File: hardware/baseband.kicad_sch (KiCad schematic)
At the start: 3 parts

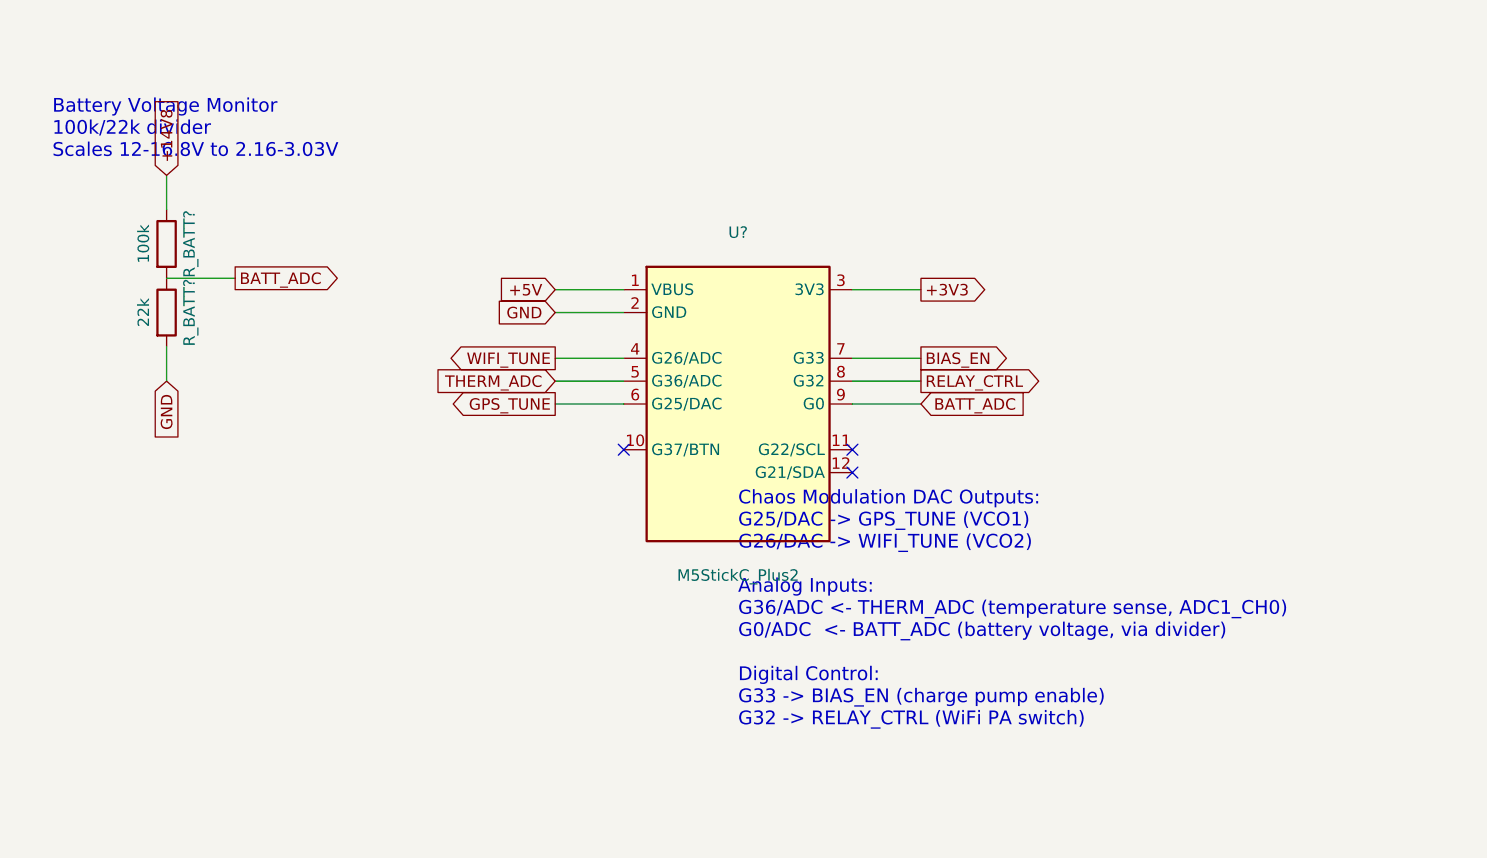
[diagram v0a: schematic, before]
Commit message: jamrf-v2: Add U3V70F15 WiFi PA regulator, FR408HR stackup, full firmware, custom footprints
- Add U3V70F15 buck-boost converter to limit WiFi PA supply to 15V (fixes ZVE-3W-83+ overvoltage)
- Update PCB stackup to Isola FR408HR (Er=3.65, tan d=0.0095) with corrected 0.40mm 50-ohm traces
- Add full operational firmware (main.py): chaos modulation engine, ST7789 display, mode control
- Add 6 custom footprints: M5StickC, Pololu D24V10F5/U3V70F15, Mini-Circuits, Wurth shield, isolator
- Add fp-lib-table and sym-lib-table for custom libraries
- Update README with logo, badges, TIIUAE disclaimer, corrected specs
- Update LICENSE with proper attribution

Co-Authored-By: Claude Opus 4.6 <noreply@anthropic.com>
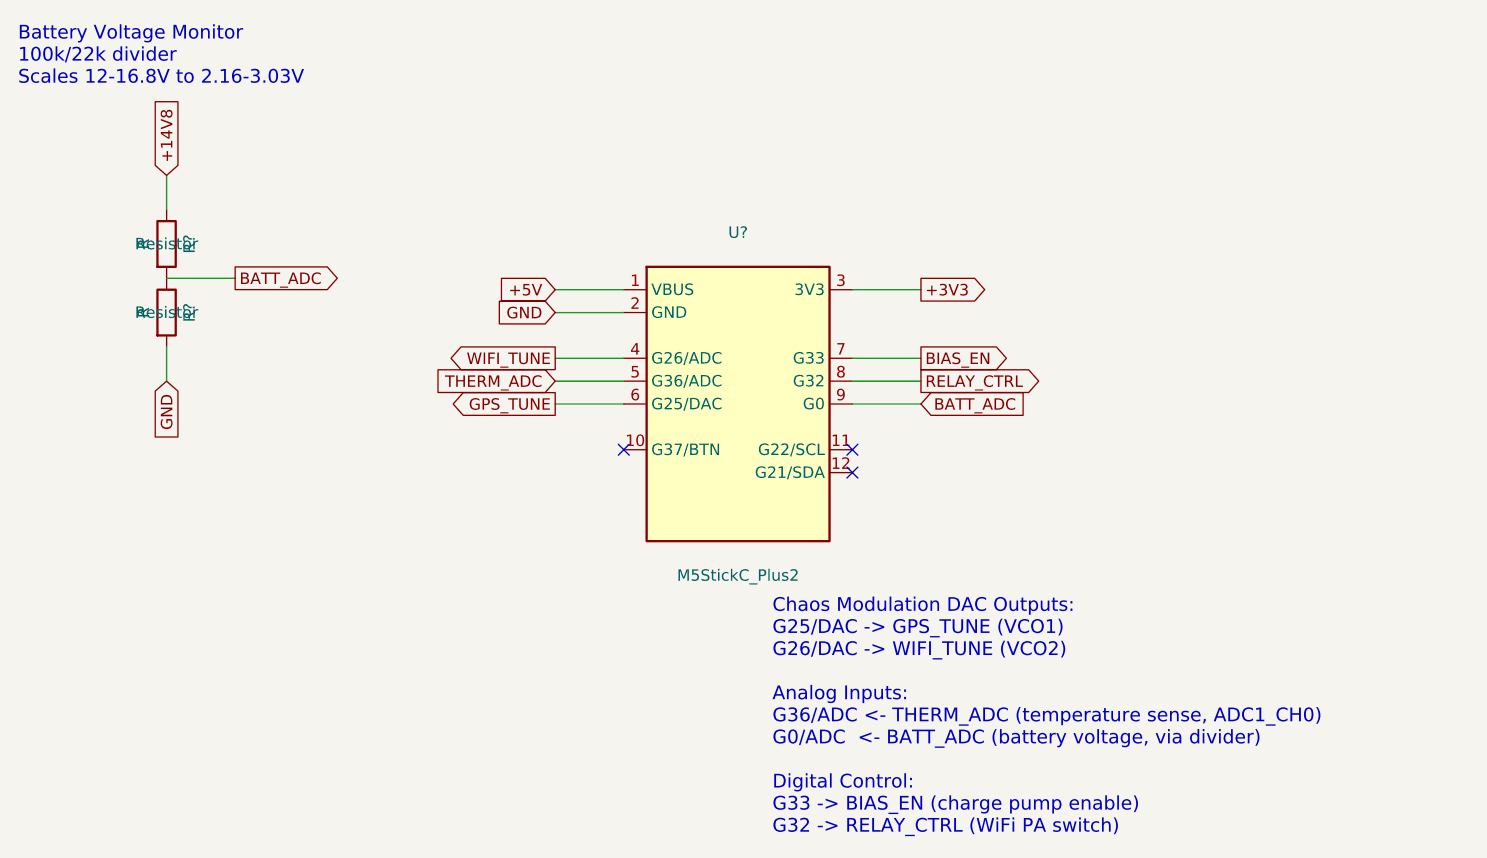
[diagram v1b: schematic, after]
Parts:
- R?: renamed from R_BATT?; value 100k -> R
- R?: renamed from R_BATT?; value 22k -> R
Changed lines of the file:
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@@
 	(text "Battery Voltage Monitor\n100k/22k divider\nScales 12-16.8V to 2.16-3.03V"
 		(exclude_from_sim no)
-		(at 63.5 58.42 0)
+		(at 59.69 50.292 0)
 		(effects
 			(font
@@
 	(text "Chaos Modulation DAC Outputs:\nG25/DAC -> GPS_TUNE (VCO1)\nG26/DAC -> WIFI_TUNE (VCO2)\n\nAnalog Inputs:\nG36/ADC <- THERM_ADC (temperature sense, ADC1_CH0)\nG0/ADC  <- BATT_ADC (battery voltage, via divider)\n\nDigital Control:\nG33 -> BIAS_EN (charge pump enable)\nG32 -> RELAY_CTRL (WiFi PA switch)"
 		(exclude_from_sim no)
-		(at 139.7 111.76 0)
+		(at 143.51 123.698 0)
 		(effects
 			(font
@@
 			(width 0)
 			(type default)
+		)
+	)
+	(global_label "+5V"
+		(shape input)
+		(at 119.38 76.2 180)
+		(effects
+			(font
+				(size 1.27 1.27)
+			)
+			(justify right)
+		)
+		(property "Intersheetrefs" "${INTERSHEET_REFS}"
+			(at 119.38 76.2 0)
+			(effects
+				(font
+					(size 1.27 1.27)
+				)
+				(hide yes)
+			)
+		)
+	)
+	(global_label "GND"
+		(shape input)
+		(at 119.38 78.74 180)
+		(effects
+			(font
+				(size 1.27 1.27)
+			)
+			(justify right)
+		)
+		(property "Intersheetrefs" "${INTERSHEET_REFS}"
+			(at 119.38 78.74 0)
+			(effects
+				(font
+					(size 1.27 1.27)
+				)
+				(hide yes)
+			)
+		)
+	)
+	(global_label "+3V3"
+		(shape output)
+		(at 160.02 76.2 0)
+		(effects
+			(font
+				(size 1.27 1.27)
+			)
+			(justify left)
+		)
+		(property "Intersheetrefs" "${INTERSHEET_REFS}"
+			(at 160.02 76.2 0)
+			(effects
+				(font
+					(size 1.27 1.27)
+				)
+				(hide yes)
+			)
+		)
+	)
+	(global_label "WIFI_TUNE"
+		(shape output)
+		(at 119.38 83.82 180)
+		(effects
+			(font
+				(size 1.27 1.27)
+			)
+			(justify right)
+		)
+		(property "Intersheetrefs" "${INTERSHEET_REFS}"
+			(at 119.38 83.82 0)
+			(effects
+				(font
+					(size 1.27 1.27)
+				)
+				(hide yes)
+			)
 		)
 	)
@@
 		)
 	)
+	(global_label "GPS_TUNE"
+		(shape output)
+		(at 119.38 88.9 180)
+		(effects
+			(font
+				(size 1.27 1.27)
+			)
+			(justify right)
+		)
+		(property "Intersheetrefs" "${INTERSHEET_REFS}"
+			(at 119.38 88.9 0)
+			(effects
+				(font
+					(size 1.27 1.27)
+				)
+				(hide yes)
+			)
+		)
+	)
+	(global_label "BIAS_EN"
+		(shape output)
+		(at 160.02 83.82 0)
+		(effects
+			(font
+				(size 1.27 1.27)
+			)
+			(justify left)
+		)
+		(property "Intersheetrefs" "${INTERSHEET_REFS}"
+			(at 160.02 83.82 0)
+			(effects
+				(font
+					(size 1.27 1.27)
+				)
+				(hide yes)
+			)
+		)
+	)
+	(global_label "RELAY_CTRL"
+		(shape output)
+		(at 160.02 86.36 0)
+		(effects
+			(font
+				(size 1.27 1.27)
+			)
+			(justify left)
+		)
+		(property "Intersheetrefs" "${INTERSHEET_REFS}"
+			(at 160.02 86.36 0)
+			(effects
+				(font
+					(size 1.27 1.27)
+				)
+				(hide yes)
+			)
+		)
+	)
+	(global_label "BATT_ADC"
+		(shape input)
+		(at 160.02 88.9 0)
+		(effects
+			(font
+				(size 1.27 1.27)
+			)
+			(justify left)
+		)
+		(property "Intersheetrefs" "${INTERSHEET_REFS}"
+			(at 160.02 88.9 0)
+			(effects
+				(font
+					(size 1.27 1.27)
+				)
+				(hide yes)
+			)
+		)
+	)
+	(global_label "+14V8"
+		(shape input)
+		(at 76.2 63.5 90)
+		(effects
+			(font
+				(size 1.27 1.27)
+			)
+			(justify left)
+		)
+		(property "Intersheetrefs" "${INTERSHEET_REFS}"
+			(at 76.2 63.5 0)
+			(effects
+				(font
+					(size 1.27 1.27)
+				)
+				(hide yes)
+			)
+		)
+	)
 	(global_label "BATT_ADC"
 		(shape output)
@@
 		(property "Intersheetrefs" "${INTERSHEET_REFS}"
 			(at 83.82 74.93 0)
-			(effects
-				(font
-					(size 1.27 1.27)
-				)
-				(hide yes)
-			)
-		)
-	)
-	(global_label "+5V"
-		(shape input)
-		(at 119.38 76.2 180)
-		(effects
-			(font
-				(size 1.27 1.27)
-			)
-			(justify right)
-		)
-		(property "Intersheetrefs" "${INTERSHEET_REFS}"
-			(at 119.38 76.2 0)
-			(effects
-				(font
-					(size 1.27 1.27)
-				)
-				(hide yes)
-			)
-		)
-	)
-	(global_label "GND"
-		(shape input)
-		(at 119.38 78.74 180)
-		(effects
-			(font
-				(size 1.27 1.27)
-			)
-			(justify right)
-		)
-		(property "Intersheetrefs" "${INTERSHEET_REFS}"
-			(at 119.38 78.74 0)
-			(effects
-				(font
-					(size 1.27 1.27)
-				)
-				(hide yes)
-			)
-		)
-	)
-	(global_label "+3V3"
-		(shape output)
-		(at 160.02 76.2 0)
-		(effects
-			(font
-				(size 1.27 1.27)
-			)
-			(justify left)
-		)
-		(property "Intersheetrefs" "${INTERSHEET_REFS}"
-			(at 160.02 76.2 0)
-			(effects
-				(font
-					(size 1.27 1.27)
-				)
-				(hide yes)
-			)
-		)
-	)
-	(global_label "WIFI_TUNE"
-		(shape output)
-		(at 119.38 83.82 180)
-		(effects
-			(font
-				(size 1.27 1.27)
-			)
-			(justify right)
-		)
-		(property "Intersheetrefs" "${INTERSHEET_REFS}"
-			(at 119.38 83.82 0)
-			(effects
-				(font
-					(size 1.27 1.27)
-				)
-				(hide yes)
-			)
-		)
-	)
-	(global_label "GPS_TUNE"
-		(shape output)
-		(at 119.38 88.9 180)
-		(effects
-			(font
-				(size 1.27 1.27)
-			)
-			(justify right)
-		)
-		(property "Intersheetrefs" "${INTERSHEET_REFS}"
-			(at 119.38 88.9 0)
-			(effects
-				(font
-					(size 1.27 1.27)
-				)
-				(hide yes)
-			)
-		)
-	)
-	(global_label "BIAS_EN"
-		(shape output)
-		(at 160.02 83.82 0)
-		(effects
-			(font
-				(size 1.27 1.27)
-			)
-			(justify left)
-		)
-		(property "Intersheetrefs" "${INTERSHEET_REFS}"
-			(at 160.02 83.82 0)
-			(effects
-				(font
-					(size 1.27 1.27)
-				)
-				(hide yes)
-			)
-		)
-	)
-	(global_label "RELAY_CTRL"
-		(shape output)
-		(at 160.02 86.36 0)
-		(effects
-			(font
-				(size 1.27 1.27)
-			)
-			(justify left)
-		)
-		(property "Intersheetrefs" "${INTERSHEET_REFS}"
-			(at 160.02 86.36 0)
-			(effects
-				(font
-					(size 1.27 1.27)
-				)
-				(hide yes)
-			)
-		)
-	)
-	(global_label "BATT_ADC"
-		(shape input)
-		(at 160.02 88.9 0)
-		(effects
-			(font
-				(size 1.27 1.27)
-			)
-			(justify left)
-		)
-		(property "Intersheetrefs" "${INTERSHEET_REFS}"
-			(at 160.02 88.9 0)
-			(effects
-				(font
-					(size 1.27 1.27)
-				)
-				(hide yes)
-			)
-		)
-	)
-	(global_label "+14V8"
-		(shape input)
-		(at 76.2 63.5 90)
-		(effects
-			(font
-				(size 1.27 1.27)
-			)
-			(justify left)
-		)
-		(property "Intersheetrefs" "${INTERSHEET_REFS}"
-			(at 76.2 63.5 0)
 			(effects
 				(font
@@
 		(on_board yes)
 		(dnp no)
-		(property "Reference" "R_BATT?"
+		(property "Reference" "R?"
 			(at 78.74 71.12 90)
 			(effects
@@
 			)
 		)
-		(property "Value" "100k"
+		(property "Value" "R"
 			(at 73.66 71.12 90)
 			(effects
@@
 			)
 		)
-		(property "Description" ""
+		(property "Description" "Resistor"
 			(at 76.2 71.12 0)
 			(effects
@@
 			(project "jamrf-v2"
 				(path "/b0000001-0000-0000-0000-000000000001/b0000001-0000-0000-0000-000000000010"
-					(reference "R_BATT?")
+					(reference "R?")
 					(unit 1)
 				)
@@
 		(on_board yes)
 		(dnp no)
-		(property "Reference" "R_BATT?"
+		(property "Reference" "R?"
 			(at 78.74 78.74 90)
 			(effects
@@
 			)
 		)
-		(property "Value" "22k"
+		(property "Value" "R"
 			(at 73.66 78.74 90)
 			(effects
@@
 			)
 		)
-		(property "Description" ""
+		(property "Description" "Resistor"
 			(at 76.2 78.74 0)
 			(effects
@@
 			(project "jamrf-v2"
 				(path "/b0000001-0000-0000-0000-000000000001/b0000001-0000-0000-0000-000000000010"
-					(reference "R_BATT?")
+					(reference "R?")
 					(unit 1)
 				)

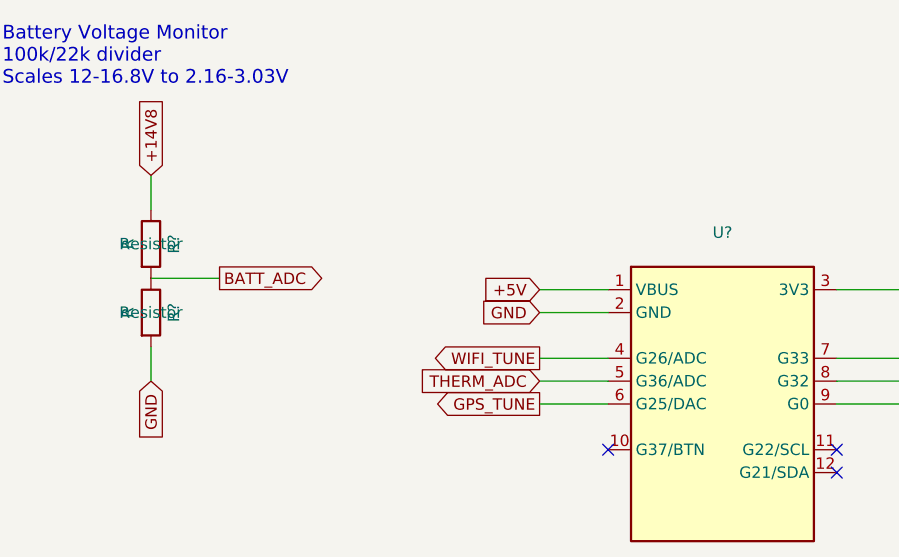
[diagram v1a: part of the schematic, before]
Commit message: Annotate all component references and update CLAUDE.md
- All component references annotated (U1-U10, R1-R17, C1-C19, Q1-Q4, etc.)
- Fix CLAUDE.md: correct jamrf-v4 description (dual-band, not WiFi-only)
- Update CLAUDE.md: file paths match main branch structure, add firmware docs
- Remove resolved known issues (annotation, footprint library)

Co-Authored-By: Claude Opus 4.6 <noreply@anthropic.com>
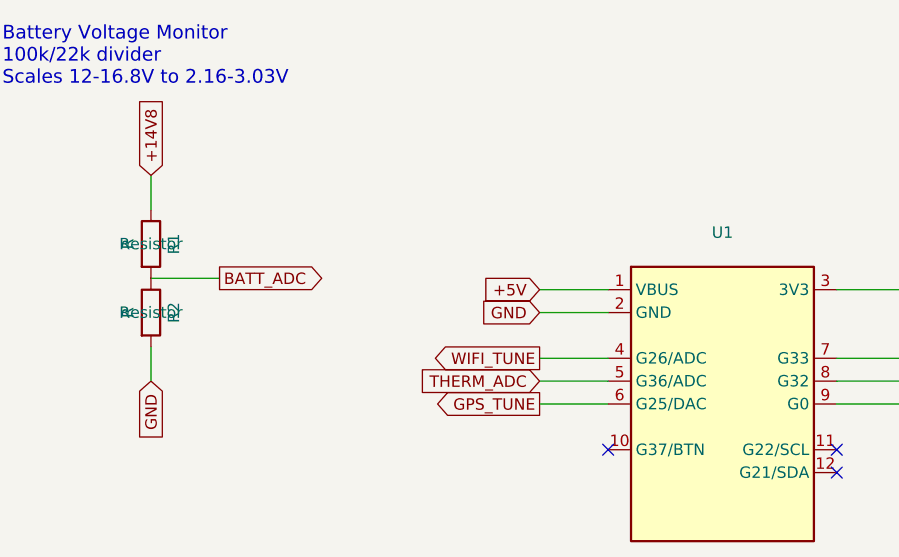
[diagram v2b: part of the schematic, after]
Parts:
- gave numbers to parts that had none: 3
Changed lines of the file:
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@@
 		(on_board yes)
 		(dnp no)
-		(property "Reference" "U?"
+		(property "Reference" "U1"
 			(at 139.7 69.85 0)
 			(effects
@@
 			(project "jamrf-v2"
 				(path "/b0000001-0000-0000-0000-000000000001/b0000001-0000-0000-0000-000000000010"
-					(reference "U?")
+					(reference "U1")
 					(unit 1)
 				)
@@
 		(on_board yes)
 		(dnp no)
-		(property "Reference" "R?"
+		(property "Reference" "R1"
 			(at 78.74 71.12 90)
 			(effects
@@
 			(project "jamrf-v2"
 				(path "/b0000001-0000-0000-0000-000000000001/b0000001-0000-0000-0000-000000000010"
-					(reference "R?")
+					(reference "R1")
 					(unit 1)
 				)
@@
 		(on_board yes)
 		(dnp no)
-		(property "Reference" "R?"
+		(property "Reference" "R2"
 			(at 78.74 78.74 90)
 			(effects
@@
 			(project "jamrf-v2"
 				(path "/b0000001-0000-0000-0000-000000000001/b0000001-0000-0000-0000-000000000010"
-					(reference "R?")
+					(reference "R2")
 					(unit 1)
 				)
